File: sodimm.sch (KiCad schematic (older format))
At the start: 1 part, among them J5 2309409-1

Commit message: Equalize lenghts of DDR CA
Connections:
- net labels added: IO_N5
- wire segments 227 -> 228
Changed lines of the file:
@@
 Wire Wire Line
 	8075 8600 8075 8700
+Text GLabel 11775 5075 2    50   Input ~ 0
+IO_N5
+Wire Wire Line
+	11350 5075 11775 5075
 $EndSCHEMATC

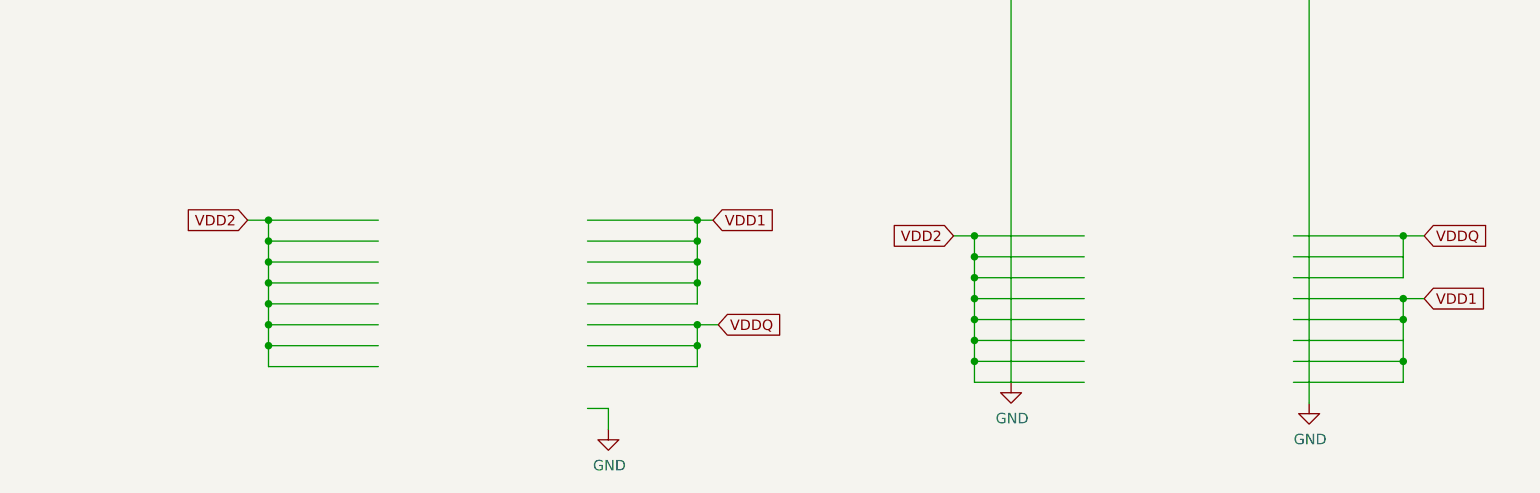
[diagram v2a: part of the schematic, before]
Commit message: Introduce unified 1V1_SYS 1V8_SYS 3V3_SYS
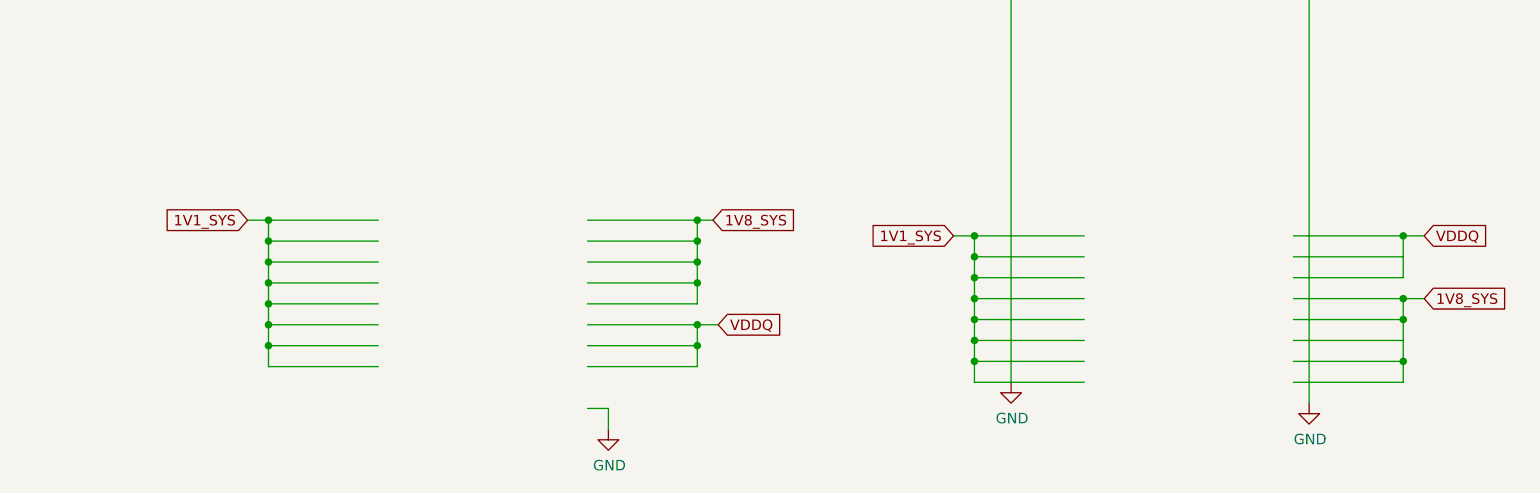
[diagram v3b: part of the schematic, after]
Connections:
- net labels added: 1V1_SYS, 1V8_SYS
- net labels removed: VDD1, VDD2
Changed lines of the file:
@@
 	6350 7700 6450 7700
 Text GLabel 6350 7700 0    50   Input ~ 0
-VDD2
+1V1_SYS
 $Comp
 L antmicroMemoryConnectorsPCCardSockets:2309409-1 J5
@@
 	9725 7775 9825 7775
 Text GLabel 9725 7775 0    50   Input ~ 0
-VDD2
+1V1_SYS
 Wire Wire Line
 	10350 7775 9825 7775
@@
 	11975 7775 11875 7775
 Text GLabel 11975 8075 2    50   Input ~ 0
-VDD1
+1V8_SYS
 Wire Wire Line
 	11350 8275 11875 8275
@@
 	8600 8200 8500 8200
 Text GLabel 8575 7700 2    50   Input ~ 0
-VDD1
+1V8_SYS
 Connection ~ 8500 7800
 Wire Wire Line

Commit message: Update component library
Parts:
- J5: footprint antmicro-footprints:TE_2309409-1 -> lpddr4-test-board-footprints:TE_2309409-1; symbol antmicroMemoryConnectorsPCCardSockets:2309409-1 -> lpddr4-test-board:2309409-1
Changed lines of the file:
@@
 DQ11_A
 $Comp
-L antmicroMemoryConnectorsPCCardSockets:2309409-1 J5
+L lpddr4-test-board:2309409-1 J5
 U 2 1 5FCC3654
 P 10850 5275
 F 0 "J5" H 10850 8742 50  0000 C CNN
 F 1 "2309409-1" H 10850 8651 50  0000 C CNN
-F 2 "antmicro-footprints:TE_2309409-1" H 10550 1675 50  0001 L BNN
+F 2 "lpddr4-test-board-footprints:TE_2309409-1" H 10550 1675 50  0001 L BNN
 F 3 "" H 11850 5375 50  0001 L BNN
 	2    10850 5275
@@
 1V1_SYS
 $Comp
-L antmicroMemoryConnectorsPCCardSockets:2309409-1 J5
+L lpddr4-test-board:2309409-1 J5
 U 1 1 5FC76C01
 P 7475 5300
 F 0 "J5" H 7475 8867 50  0000 C CNN
 F 1 "2309409-1" H 7475 8776 50  0000 C CNN
-F 2 "antmicro-footprints:TE_2309409-1" H 7175 1700 50  0001 L BNN
+F 2 "lpddr4-test-board-footprints:TE_2309409-1" H 7175 1700 50  0001 L BNN
 F 3 "" H 8475 5400 50  0001 L BNN
 	1    7475 5300

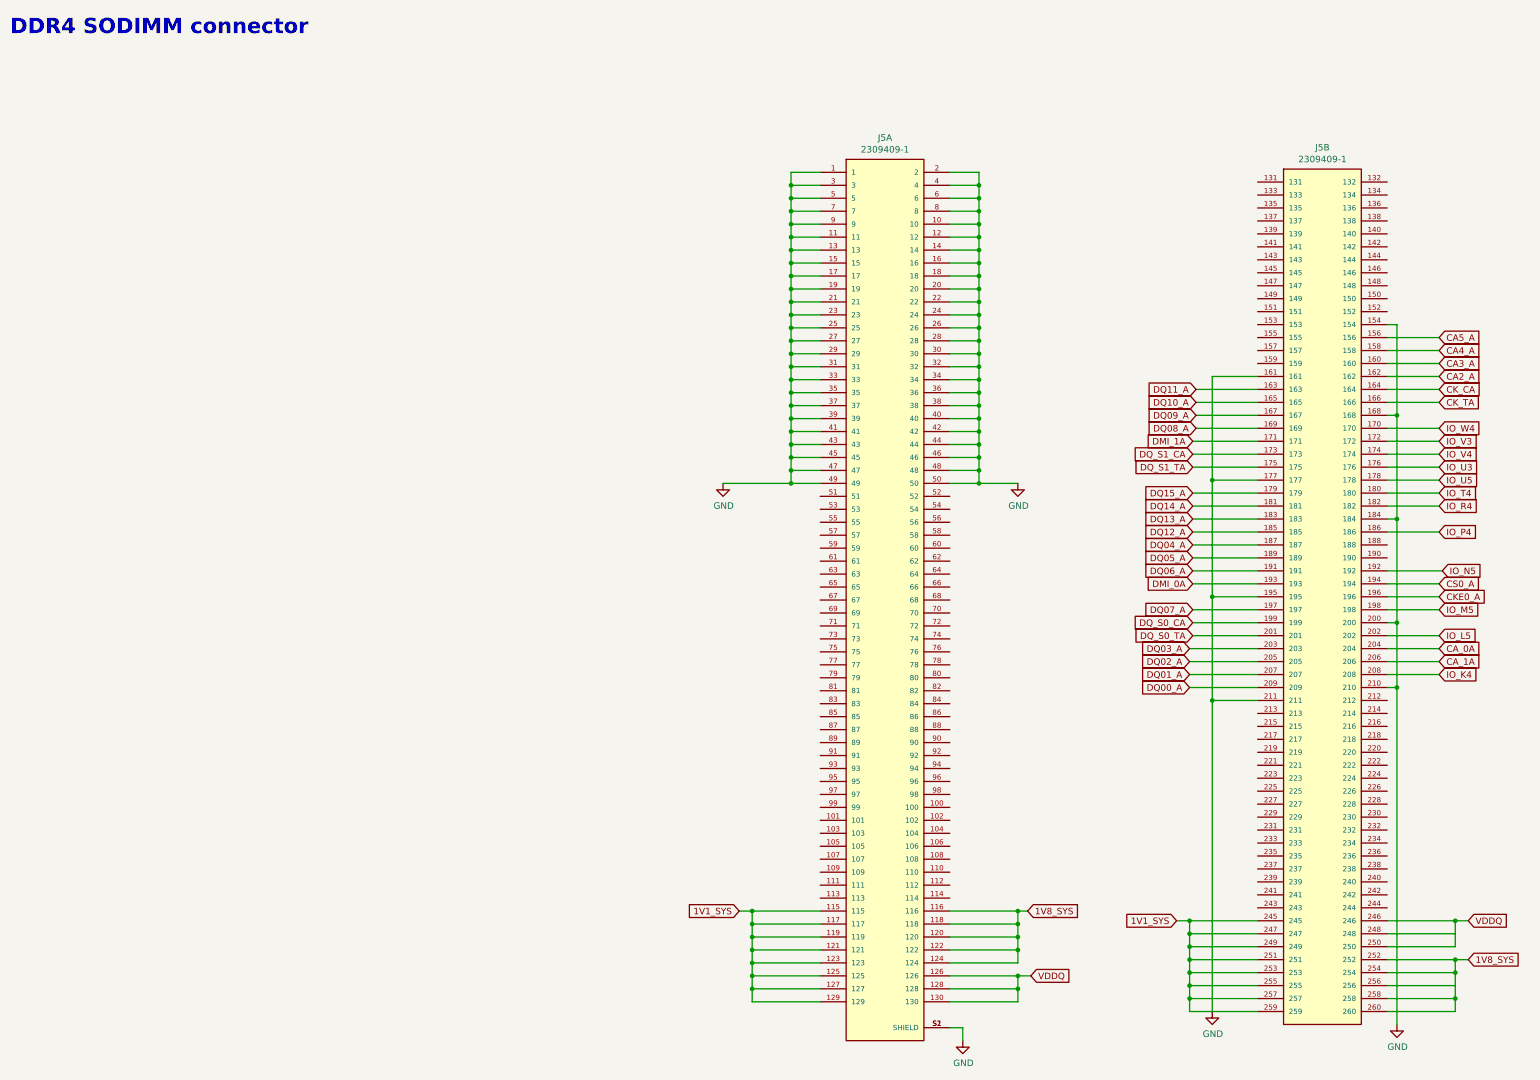
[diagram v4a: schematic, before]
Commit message: Reconnect AUX_JTAG + UART, Connect spare IOs to the SODIMM
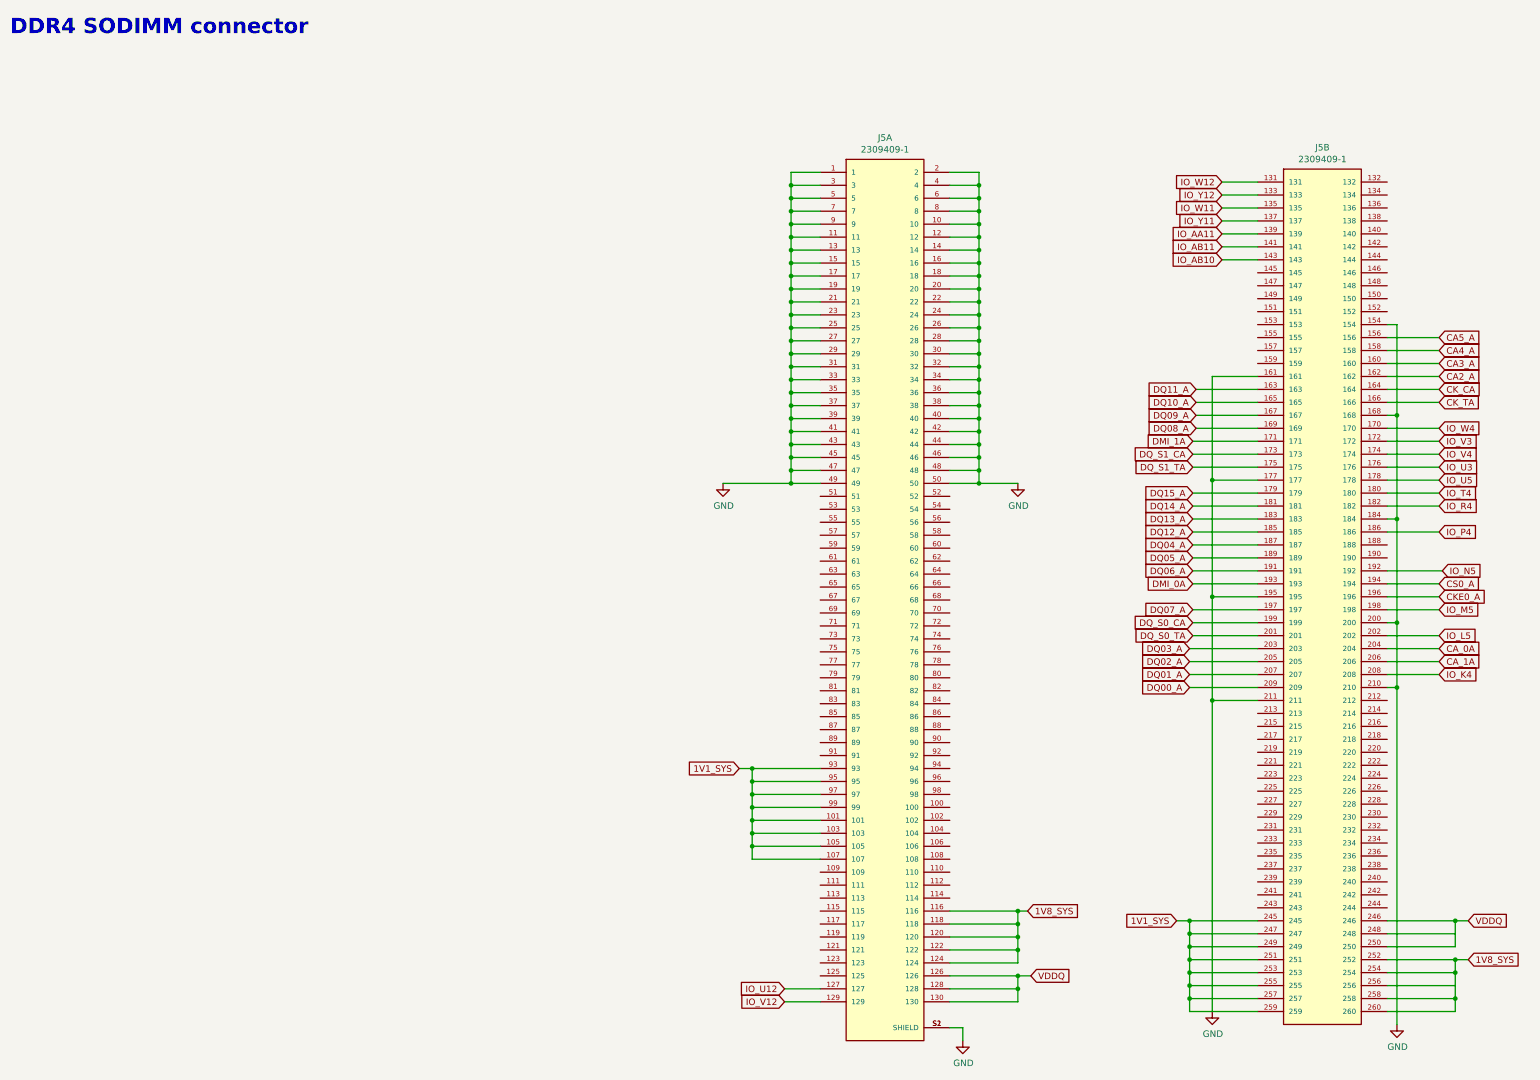
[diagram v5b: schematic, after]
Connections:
- net 1V1_SYS: now also J5.101, J5.103, J5.105, J5.107, J5.93, J5.95, J5.97, J5.99; no longer J5.115, J5.117, J5.119, J5.121, J5.123, J5.125, J5.127, J5.129
- net IO_W12: now reaches J5.131
- net IO_Y12: now reaches J5.133
- net IO_W11: now reaches J5.135
- net IO_Y11: now reaches J5.137
- net IO_AA11: now reaches J5.139
- net IO_AB11: now reaches J5.141
- net IO_AB10: now reaches J5.143
- new net IO_U12: J5.127
- new net IO_V12: J5.129
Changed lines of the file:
@@
 	8200 4400 8500 4400
 Wire Wire Line
-	6450 8000 6975 8000
-Wire Wire Line
-	6975 7800 6450 7800
-Wire Wire Line
-	6975 8200 6450 8200
-Wire Wire Line
-	6975 8100 6450 8100
-Wire Wire Line
-	6975 7900 6450 7900
-Wire Wire Line
-	6975 8300 6450 8300
-Connection ~ 6450 7800
-Wire Wire Line
-	6450 7800 6450 7900
-Connection ~ 6450 7900
-Wire Wire Line
-	6450 7900 6450 8000
-Connection ~ 6450 8100
-Wire Wire Line
-	6450 8100 6450 8200
-Connection ~ 6450 8200
-Wire Wire Line
-	6450 8200 6450 8300
-Wire Wire Line
-	6975 8400 6450 8400
+	6450 6900 6975 6900
+Wire Wire Line
+	6975 6700 6450 6700
+Wire Wire Line
+	6975 7100 6450 7100
+Wire Wire Line
+	6975 7000 6450 7000
+Wire Wire Line
+	6975 6800 6450 6800
+Wire Wire Line
+	6975 7200 6450 7200
+Connection ~ 6450 6700
+Wire Wire Line
+	6450 6700 6450 6800
+Connection ~ 6450 6800
+Wire Wire Line
+	6450 6800 6450 6900
+Connection ~ 6450 7000
+Wire Wire Line
+	6450 7000 6450 7100
+Connection ~ 6450 7100
+Wire Wire Line
+	6450 7100 6450 7200
+Wire Wire Line
+	6975 7300 6450 7300
 Text GLabel 9875 3675 0    50   Input ~ 0
 DQ11_A
@@
 Wire Wire Line
 	11425 5475 11425 5975
-Connection ~ 6450 8000
-Wire Wire Line
-	6450 8000 6450 8100
-Connection ~ 6450 8300
-Wire Wire Line
-	6450 8300 6450 8400
-Wire Wire Line
-	6350 7700 6450 7700
-Text GLabel 6350 7700 0    50   Input ~ 0
+Connection ~ 6450 6900
+Wire Wire Line
+	6450 6900 6450 7000
+Connection ~ 6450 7200
+Wire Wire Line
+	6450 7200 6450 7300
+Wire Wire Line
+	6350 6600 6450 6600
+Text GLabel 6350 6600 0    50   Input ~ 0
 1V1_SYS
 $Comp
@@
 	8200 4200 8200 4300
 Wire Wire Line
-	6975 7700 6450 7700
-Wire Wire Line
-	6450 7700 6450 7800
-Connection ~ 6450 7700
+	6975 6600 6450 6600
+Wire Wire Line
+	6450 6600 6450 6700
+Connection ~ 6450 6600
 Wire Wire Line
 	9825 8075 10350 8075
@@
 Wire Wire Line
 	11350 5075 11775 5075
+Text GLabel 10075 2675 0    50   Input ~ 0
+IO_AB10
+Text GLabel 10075 2575 0    50   Input ~ 0
+IO_AB11
+Text GLabel 10075 2475 0    50   Input ~ 0
+IO_AA11
+Text GLabel 10075 2375 0    50   Input ~ 0
+IO_Y11
+Text GLabel 10075 2275 0    50   Input ~ 0
+IO_W11
+Text GLabel 10075 2175 0    50   Input ~ 0
+IO_Y12
+Text GLabel 10075 2075 0    50   Input ~ 0
+IO_W12
+Wire Wire Line
+	10075 2075 10350 2075
+Wire Wire Line
+	10075 2175 10350 2175
+Wire Wire Line
+	10075 2275 10350 2275
+Wire Wire Line
+	10075 2375 10350 2375
+Wire Wire Line
+	10075 2475 10350 2475
+Wire Wire Line
+	10075 2575 10350 2575
+Wire Wire Line
+	10075 2675 10350 2675
+Text GLabel 6700 8400 0    50   Input ~ 0
+IO_V12
+Text GLabel 6700 8300 0    50   Input ~ 0
+IO_U12
+Wire Wire Line
+	6700 8300 6975 8300
+Wire Wire Line
+	6975 8400 6700 8400
 $EndSCHEMATC

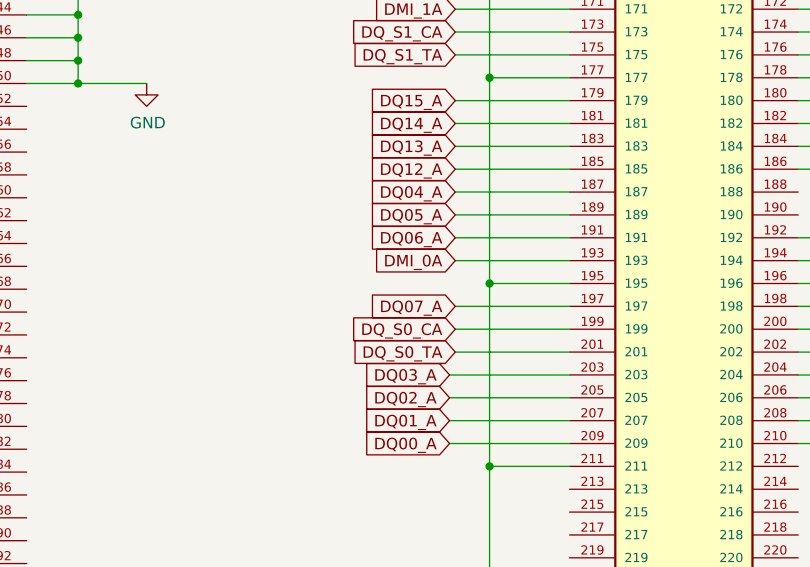
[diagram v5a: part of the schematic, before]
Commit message: SWAP DQ_07A with DMI_0A
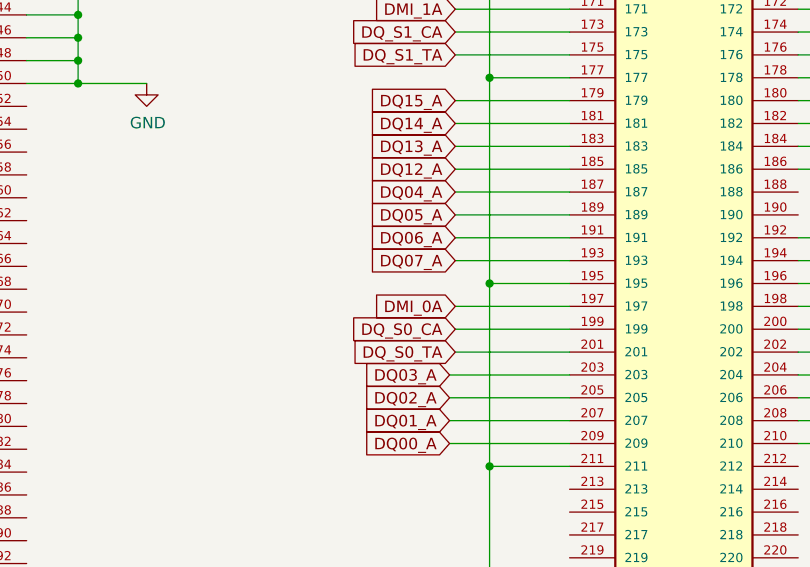
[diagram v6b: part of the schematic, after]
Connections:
- net DMI_0A: now also J5.197; no longer J5.193
- net DQ07_A: now also J5.193; no longer J5.197
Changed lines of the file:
@@
 Text GLabel 9850 5075 0    50   Input ~ 0
 DQ06_A
-Text GLabel 9850 5375 0    50   Input ~ 0
+Text GLabel 9850 5175 0    50   Input ~ 0
 DQ07_A
 Text GLabel 9850 5475 0    50   Input ~ 0
@@
 Wire Wire Line
 	9850 4075 10350 4075
-Text GLabel 9850 5175 0    50   Input ~ 0
+Text GLabel 9850 5375 0    50   Input ~ 0
 DMI_0A
 Text GLabel 9850 5575 0    50   Input ~ 0

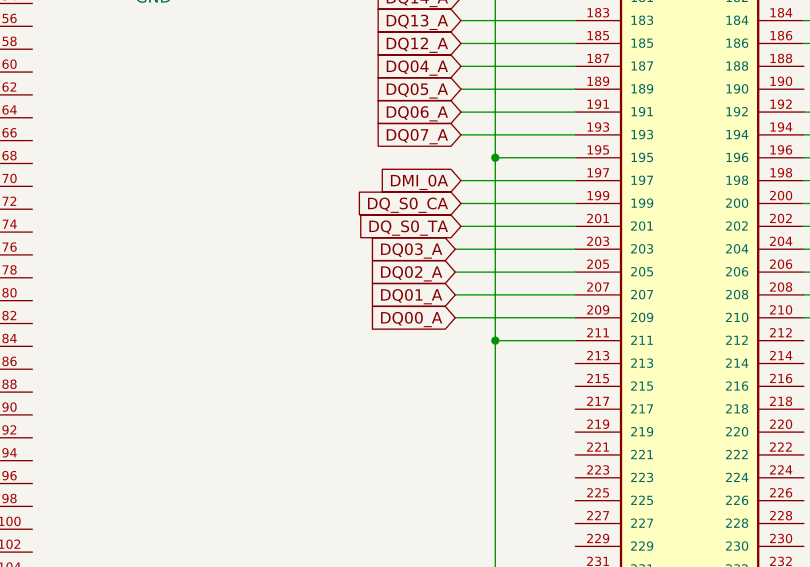
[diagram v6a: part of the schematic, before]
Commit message: Update SO-DIMM signal mapping
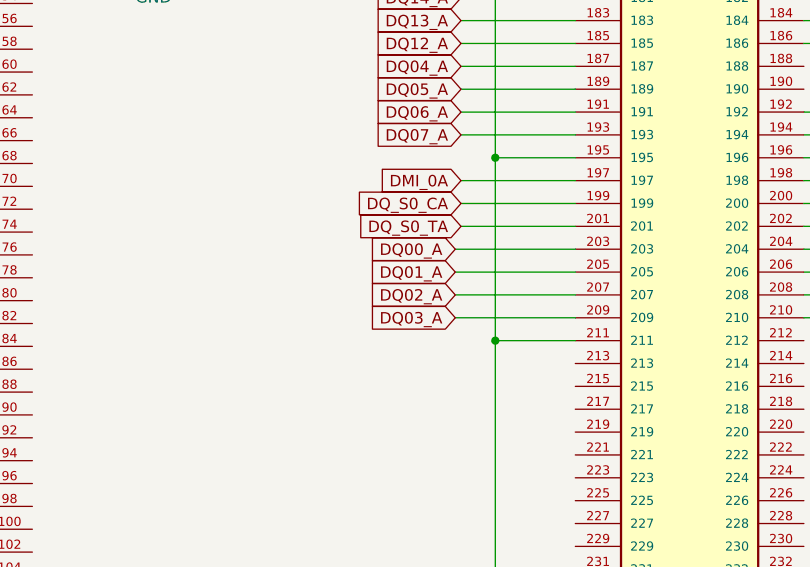
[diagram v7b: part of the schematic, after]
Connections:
- net DQ00_A: now also J5.203; no longer J5.209
- net DQ01_A: now also J5.205; no longer J5.207
- net DQ02_A: now also J5.207; no longer J5.205
- net DQ03_A: now also J5.209; no longer J5.203
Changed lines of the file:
@@
 Wire Wire Line
 	9850 5575 10350 5575
+Text GLabel 9825 5975 0    50   Input ~ 0
+DQ03_A
+Text GLabel 9825 5875 0    50   Input ~ 0
+DQ02_A
+Text GLabel 9825 5775 0    50   Input ~ 0
+DQ01_A
 Text GLabel 9825 5675 0    50   Input ~ 0
-DQ03_A
-Text GLabel 9825 5775 0    50   Input ~ 0
-DQ02_A
-Text GLabel 9825 5875 0    50   Input ~ 0
-DQ01_A
-Text GLabel 9825 5975 0    50   Input ~ 0
 DQ00_A
 Wire Wire Line
